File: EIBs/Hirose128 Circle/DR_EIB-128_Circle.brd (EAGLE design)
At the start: 38.6 x 38.6 mm, 42 parts

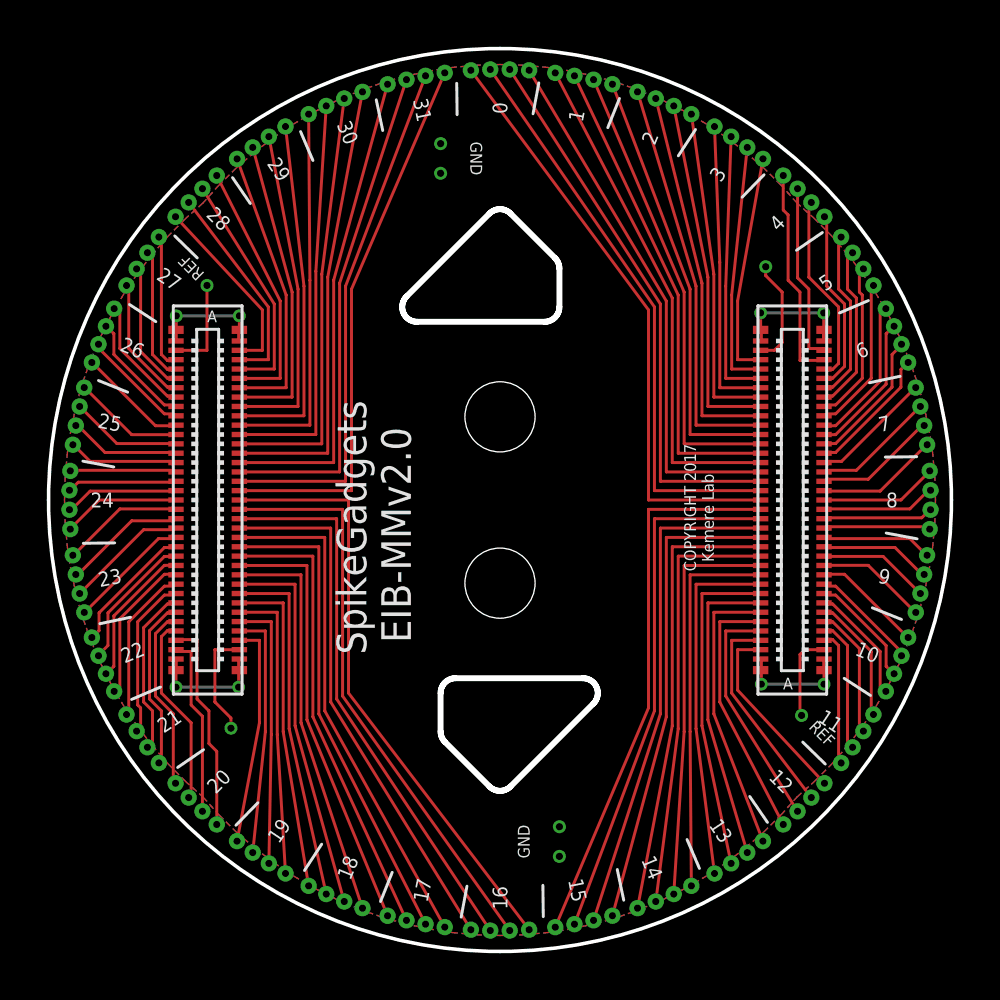
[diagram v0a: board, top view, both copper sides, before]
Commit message: Updated design to fix error
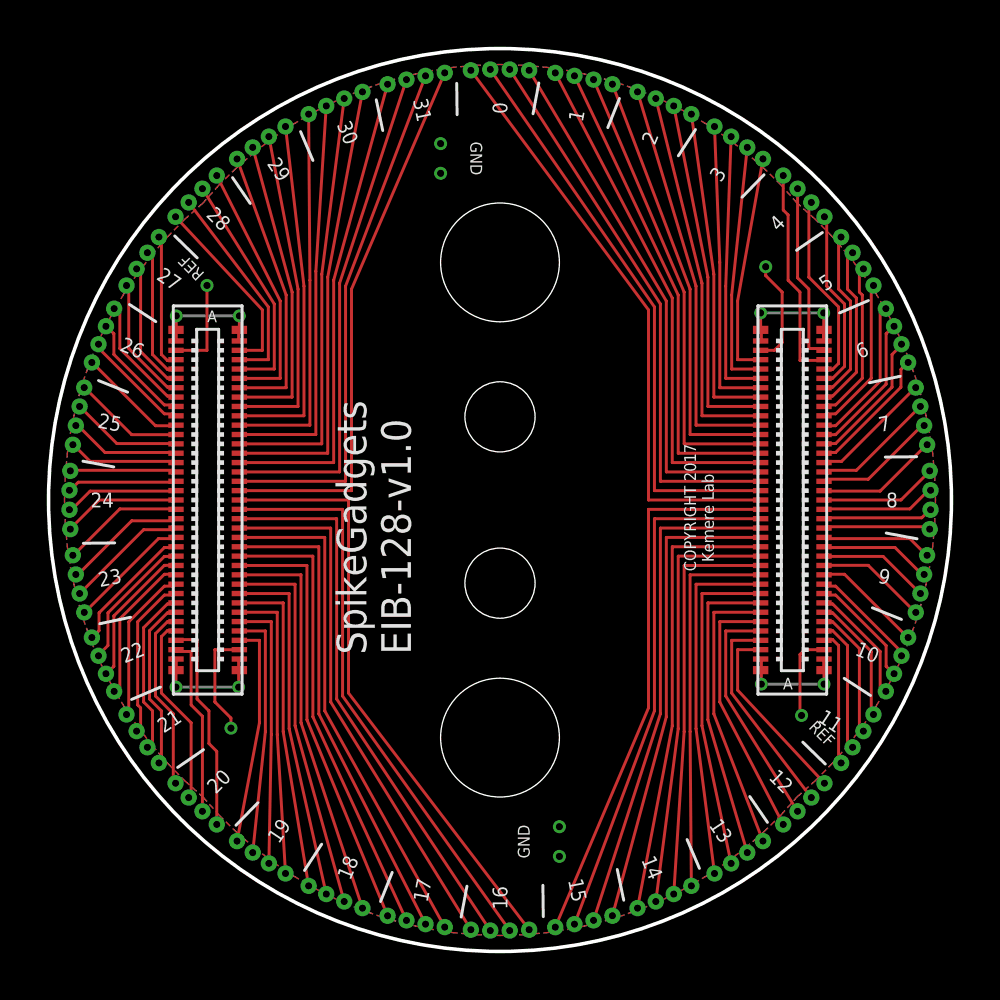
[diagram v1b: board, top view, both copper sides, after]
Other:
- outline, holes or cut-outs redrawn
- board text added: "SpikeGadgets EIB-128-v1.0"
- board text removed: "SpikeGadgets EIB-MMv2.0"
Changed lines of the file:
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@@
 <text x="36.83" y="52.705" size="0.508" layer="21" font="vector" ratio="16" rot="SR270" align="bottom-center">GND</text>
 <text x="34.29" y="31.496" size="1.27" layer="21" font="vector" ratio="10" rot="R90">SpikeGadgets
- EIB-MMv2.0</text>
+EIB-128-v1.0</text>
 <text x="47.244" y="35.052" size="0.508" layer="21" font="vector" rot="R90">COPYRIGHT 2017
   Kemere Lab</text>
-<circle x="38.1" y="34.544" radius="2.89604375" width="0.4064" layer="29"/>
-<circle x="38.1" y="41.656" radius="2.89604375" width="0.4064" layer="29"/>
+<circle x="38.1" y="34.544" radius="2.89604375" width="1.651" layer="29"/>
+<circle x="38.1" y="41.656" radius="2.89604375" width="1.651" layer="29"/>
 <text x="39.37" y="23.495" size="0.508" layer="21" font="vector" ratio="16" rot="SR90" align="bottom-center">GND</text>
 <text x="25.489803125" y="47.789196875" size="0.508" layer="21" font="vector" ratio="16" rot="SR135">REF</text>
 <text x="51.270803125" y="28.358196875" size="0.508" layer="21" font="vector" ratio="16" rot="SR315">REF</text>
 <circle x="38.1" y="38.1" radius="19.304" width="0.1524" layer="20"/>
-<polygon width="0.254" layer="20">
-<vertex x="37.6509875" y="50.3509875"/>
-<vertex x="34.1040125" y="46.8040125" curve="135"/>
-<vertex x="34.553025" y="45.72"/>
-<vertex x="40.005" y="45.72" curve="90"/>
-<vertex x="40.64" y="46.355"/>
-<vertex x="40.64" y="47.996975" curve="45"/>
-<vertex x="40.4540125" y="48.4459875"/>
-<vertex x="38.5490125" y="50.3509875" curve="90"/>
-</polygon>
-<polygon width="0.254" layer="20">
-<vertex x="41.646975" y="30.48"/>
-<vertex x="36.195" y="30.48" curve="90"/>
-<vertex x="35.56" y="29.845"/>
-<vertex x="35.56" y="28.203025" curve="45"/>
-<vertex x="35.7459875" y="27.7540125"/>
-<vertex x="37.6509875" y="25.8490125" curve="90"/>
-<vertex x="38.5490125" y="25.8490125"/>
-<vertex x="42.0959875" y="29.3959875" curve="135"/>
-</polygon>
+<hole x="38.1" y="48.26" drill="5.08"/>
+<hole x="38.1" y="27.94" drill="5.08"/>
 </plain>
 <attributes>
